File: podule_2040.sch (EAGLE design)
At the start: 58 parts, among them IC1 LT1963EST-3.3, IC2 RP2040-QFN56, IC3 SN74ALVC164245, IC4 SN74ALVC164245, U1 W25Q32FV, Y1 12MHz

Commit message: Schematic & board V1: as used for prototype fab
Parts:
- added C1: 0.1uF, rcl:C-EUC0603K
- added R12: 100K, rcl:R-EU_R0805
- added RESET: Tact sw, SparkFun-Switches:MOMENTARY-SWITCH-SPST-SMD-5.2MM-TALL
- GPIO: device SparkFun-Connectors:CONN_05 -> matt:PINHD-1X5
- J2: device SparkFun-Connectors:USB_MICRO-B_FEMALE-SMT -> SparkFun-Connectors:USB_MICRO-B_SMT
- LED1: device led:LEDCHIPLED_0805 -> led:LEDCHIPLED_1206
- SWD: device SparkFun-Connectors:CONN_04PTH -> matt:PINHD-1X4
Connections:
- removed net N$14: IC2.RUN, SWD.4
- new net RUN: C1.1, IC2.RUN, R12.1, RESET.2, SWD.4
- net +3V3: now also R12.2
- net GND: now also C1.2, RESET.1
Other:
- note added: "(c) 2021 Matt Evans"
- note added: "31 Aug 2021"
- note added: "Arc Pipe Podule"
- note added: "Licence: Creative Commons CC BY-SA 3.0 See https://creativecommons.org/licenses/by-sa/3.0/"
- note added: "v1"
- note removed: "v0.1"
- moved on the sheet: J2

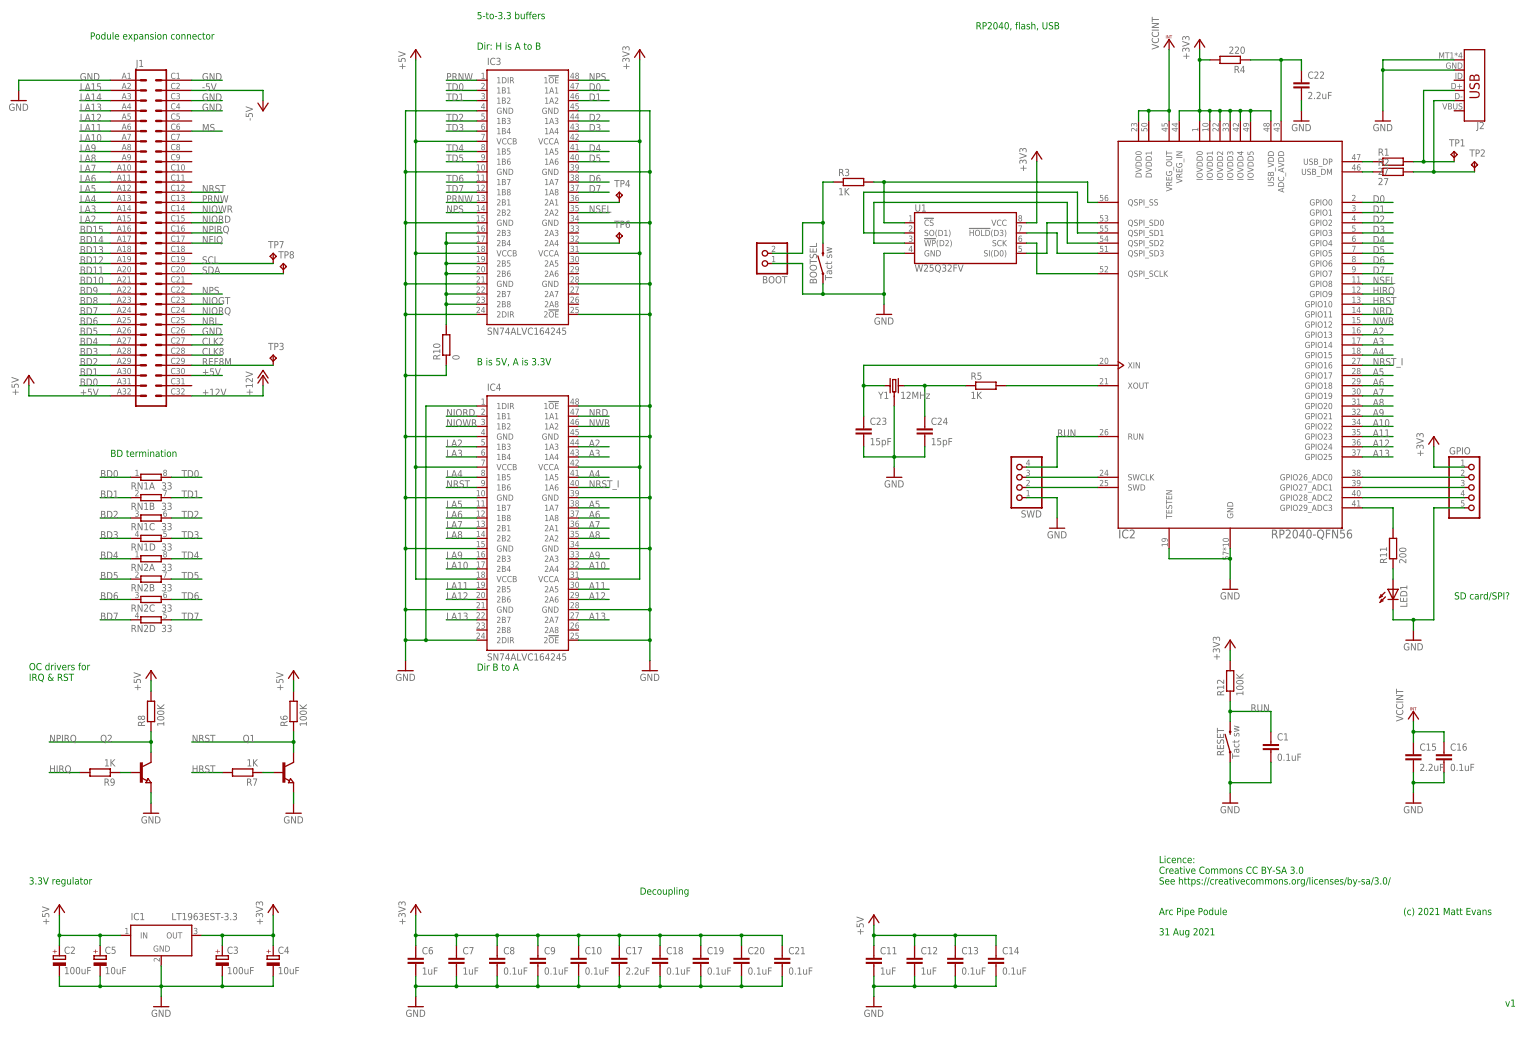
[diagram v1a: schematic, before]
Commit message: First commit of v2 design, for checking
Changes include:
- Shrink buffers to TSSOP
- Term. resistor packs on internal signals
- Removed N_RST input, freeing 4 GPIOs
- GPIOs to header, prototyping area, and added uSD footprint/resistors
- Moved QSPI closer, more decoupling, re-routed
- Brought reset/boot to a header for remote reboot
- Better labelling/silkscreen tidy, space for serial number
- More common LDO footprint
- Different crystal footprint
- Address lines contiguous
- USB VBUS can power the board, via diodes
- Flash /CS pullup footprint
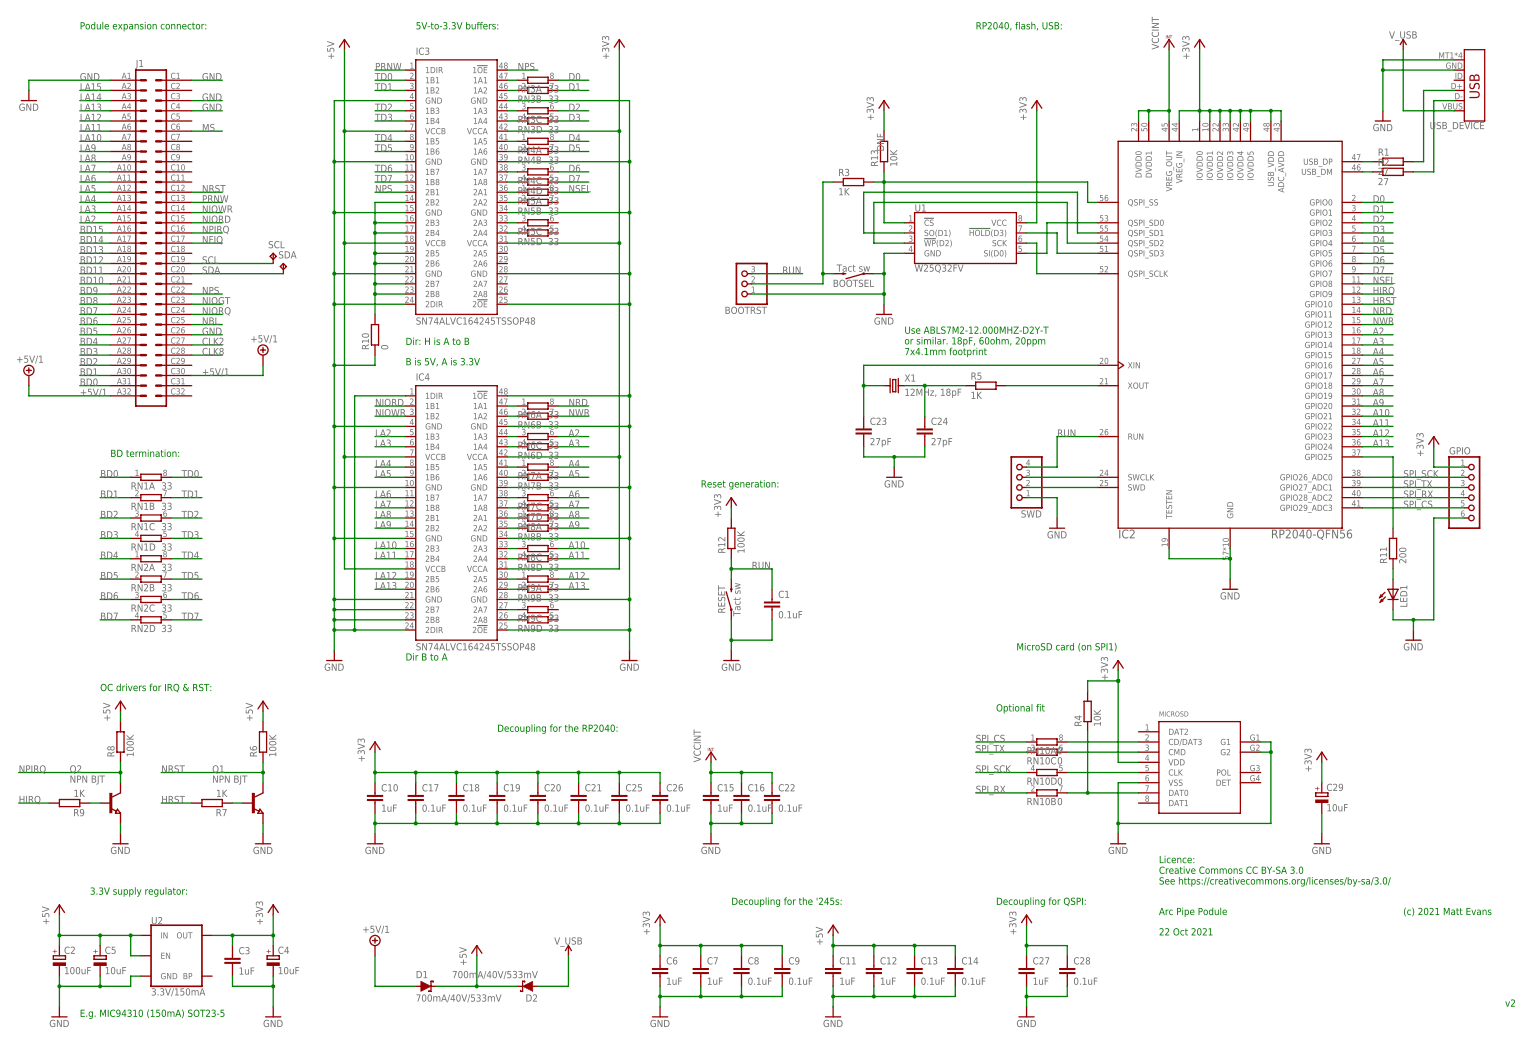
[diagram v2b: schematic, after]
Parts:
- removed BOOT: (no value), matt:PINHD-1X2
- removed IC1: LT1963EST-3.3, linear-technology:LT1963EST-3.3
- removed TP1, TP2, TP3, TP4, TP6: TPTP15R, testpad:TPTP15R
- removed Y1: 12MHz, SparkFun-Clocks:CRYSTAL-GROUNDEDSMD-5X3.2
- added BOOTRST: (no value), matt:PINHD-1X3
- added C25, C26, C28: 0.1uF, rcl:C-EUC0603K
- added C27: 1uF, rcl:C-EUC0603K
- added C29: 10uF, rcl:CPOL-EUA/3216-18W
- added D1, D2: 700mA/40V/533mV, SparkFun-DiscreteSemi:DIODE-SCHOTTKY-ZLLS500
- added MICROSD: MOLEX-USD-47309, matt:MOLEX-USD-47309
- added R13: 10K, rcl:R-EU_R0805
- added RN10: 0, resistor-dil:4R-N0603-ARC
- added RN3, RN4, RN5, RN6, RN7, RN8, RN9: 33, resistor-dil:4R-N0603-ARC
- added U2: 3.3V/150mA, SparkFun-IC-Power:V_REG_MIC52053.3V
- added X1: 12MHz, 18pF, IQD-Frequency-Products:CRYSTALS-NOGND-12SMX-A
- BOOTSEL, RESET: device SparkFun-Switches:MOMENTARY-SWITCH-SPST-SMD-5.2MM-TALL -> SparkFun-Switches:MOMENTARY-SWITCH-SPST-SMD-5.2-REDUNDANT
- C10: value 0.1uF -> 1uF
- C15: value 2.2uF -> 1uF
- C17, C22: value 2.2uF -> 0.1uF
- C23, C24: value 15pF -> 27pF
- C3: value 100uF -> 1uF; device rcl:CPOL-EUCT6032 -> rcl:C-EUC0603K
- GPIO: device matt:PINHD-1X5 -> matt:PINHD-1X6
- IC3, IC4: value SN74ALVC164245 -> SN74ALVC164245TSSOP48; device matt:SN74ALVC164245 -> matt:SN74ALVC164245TSSOP48
- Q1, Q2: value (none) -> NPN BJT
- R4: value 220 -> 10K
- renumbered J2 to USB_DEVICE, TP7 to SCL, TP8 to SDA
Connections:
- removed net +12V: J1.C32
- removed net -5V: J1.C2
- removed net N$25: GPIO.4, IC2.GPIO28_ADC2
- removed net NRST_I: IC2.GPIO16, IC4.1A6
- removed net REF8M: J1.C29, TP3.TP
- new net +5V/1: D1.A, J1.A32, J1.C30
- new net N$14: MICROSD.CD/DAT3, RN10A.2
- new net N$27: IC3.1A2, RN3B.1
- new net N$30: IC3.1A3, RN3C.1
- new net N$31: IC3.1A4, RN3D.1
- new net N$32: IC3.1A6, RN4B.1
- new net N$33: IC3.1A5, RN4A.1
- new net N$34: IC3.1A7, RN4C.1
- new net N$35: IC3.1A8, RN4D.1
- new net N$36: IC3.2A1, RN5A.1
- new net N$37: IC3.2A2, RN5B.1
- new net N$38: IC3.2A3, RN5C.1
- new net N$39: IC4.1A1, RN6A.1
- new net N$40: IC4.1A2, RN6B.1
- new net N$41: IC4.1A3, RN6C.1
- new net N$42: IC4.1A4, RN6D.1
- new net N$43: IC4.1A5, RN7A.1
- new net N$44: IC4.1A6, RN7B.1
- new net N$45: IC4.1A7, RN7C.1
- new net N$46: IC4.1A8, RN7D.1
- new net N$47: IC4.2A1, RN8A.1
- new net N$48: IC4.2A2, RN8B.1
- new net N$49: IC4.2A3, RN8C.1
- new net N$50: IC4.2A4, RN8D.1
- new net N$51: IC4.2A5, RN9A.1
- new net N$52: IC4.2A6, RN9B.1
- new net N$53: IC4.2A7, RN9C.1
- new net N$54: IC4.2A8, RN9D.1
- new net SPI_CS: GPIO.5, IC2.GPIO29_ADC3, RN10A.1
- new net SPI_RX: GPIO.4, IC2.GPIO28_ADC2, RN10B.1
- new net SPI_SCK: GPIO.2, IC2.GPIO26_ADC0, RN10D.1
- new net SPI_TX: GPIO.3, IC2.GPIO27_ADC1, RN10C.1
- new net V_USB: D2.A, USB_DEVICE.VBUS
- net +3V3: now also C25.1, C26.1, C27.1, C28.1, C29.+, C3.1, IC2.ADC_AVDD, MICROSD.VDD, R13.2, U2.OUT; no longer C3.+, IC1G$1.OUT
- net +5V: now also D1.C, D2.C, U2.EN, U2.IN; no longer IC1G$1.IN, J1.A32, J1.C30
- net A10: now also IC2.GPIO21, RN8C.2; no longer IC2.GPIO22, IC4.2A4
- net A11: now also IC2.GPIO22, RN8D.2; no longer IC2.GPIO23, IC4.2A5
- net A12: now also IC2.GPIO23, RN9A.2; no longer IC2.GPIO24, IC4.2A6
- net A13: now also IC2.GPIO24, RN9B.2; no longer IC2.GPIO25, IC4.2A7
- net A2: now also RN6C.2; no longer IC4.1A3
- net A3: now also RN6D.2; no longer IC4.1A4
- net A4: now also RN7A.2; no longer IC4.1A5
- net A5: now also IC2.GPIO16, RN7B.2; no longer IC2.GPIO17, IC4.1A7
- net A6: now also IC2.GPIO17, RN7C.2; no longer IC2.GPIO18, IC4.1A8
- net A7: now also IC2.GPIO18, RN7D.2; no longer IC2.GPIO19, IC4.2A1
- net A8: now also IC2.GPIO19, RN8A.2; no longer IC2.GPIO20, IC4.2A2
- net A9: now also IC2.GPIO20, RN8B.2; no longer IC2.GPIO21, IC4.2A3
- net D0: now also RN3A.2; no longer IC3.1A1
- net D1: now also RN3B.2; no longer IC3.1A2
- net D2: now also RN3C.2; no longer IC3.1A3
- net D3: now also RN3D.2; no longer IC3.1A4
- net D4: now also RN4A.2; no longer IC3.1A5
- net D5: now also RN4B.2; no longer IC3.1A6
- net D6: now also RN4C.2; no longer IC3.1A7
- net D7: now also RN4D.2; no longer IC3.1A8
- net GND: now also BOOTRST.1, C25.2, C26.2, C27.2, C28.2, C29.-, C3.2, GPIO.6, IC4.2B7, IC4.2B8, MICROSD.G1, MICROSD.G2, MICROSD.VSS, U2.GND; no longer BOOT.1, C3.-, GPIO.5, IC1G$1.GND, Y1.GND
- net LA10: now also IC4.2B3; no longer IC4.2B4
- net LA11: now also IC4.2B4; no longer IC4.2B5
- net LA12: now also IC4.2B5; no longer IC4.2B6
- net LA13: now also IC4.2B6; no longer IC4.2B7
- net LA5: now also IC4.1B6; no longer IC4.1B7
- net LA6: now also IC4.1B7; no longer IC4.1B8
- net LA7: now also IC4.1B8; no longer IC4.2B1
- net LA8: now also IC4.2B1; no longer IC4.2B2
- net LA9: now also IC4.2B2; no longer IC4.2B3
- net N$10: now also MICROSD.CLK, RN10D.2; no longer C22.1, IC2.ADC_AVDD, R4.1
- net N$11: now also R13.1
- net N$12: now also BOOTRST.2; no longer BOOT.2
- net N$17: now also X1.2; no longer Y1.2
- net N$19: now also X1.1; no longer Y1.1
- net N$21: now also IC3.1A1, RN3A.1; no longer IC3.2A1, TP4.TP
- net N$22: now also IC3.2B2
- net N$23: now also MICROSD.CMD, RN10C.2; no longer GPIO.2, IC2.GPIO26_ADC0
- net N$24: now also MICROSD.DAT0, R4.1, RN10B.2; no longer GPIO.3, IC2.GPIO27_ADC1
- net N$28: now also IC2.GPIO25; no longer IC2.GPIO29_ADC3
- net N$29: now also RN5D.1; no longer TP6.TP
- net N$3: no longer TP1.TP
- net N$4: no longer TP2.TP
- net NPS: now also IC3.2B1; no longer IC3.2B2
- net NRD: now also RN6A.2; no longer IC4.1A1
- net NRST: no longer IC4.1B6
- net NSEL: now also RN5A.2; no longer IC3.2A2
- net NWR: now also RN6B.2; no longer IC4.1A2
- net PRNW: no longer IC3.2B1
- net RUN: now also BOOTRST.3
- net VCCINT: now also C22.1
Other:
- note added: "22 Oct 2021"
- note added: "3.3V supply regulator:"
- note added: "5V-to-3.3V buffers:"
- note added: "BD termination:"
- note added: "Decoupling for QSPI:"
- note added: "Decoupling for the '245s:"
- note added: "Decoupling for the RP2040:"
- note added: "E.g. MIC94310 (150mA) SOT23-5"
- note added: "MicroSD card (on SPI1)"
- note added: "OC drivers for IRQ & RST:"
- note added: "Optional fit"
- note added: "Podule expansion connector:"
- note added: "RP2040, flash, USB:"
- note added: "Reset generation:"
- note added: "Use ABLS7M2-12.000MHZ-D2Y-T or similar. 18pF, 60ohm, 20ppm 7x4.1mm footprint"
- note added: "v2"
- note removed: "3.3V regulator"
- note removed: "31 Aug 2021"
- note removed: "5-to-3.3 buffers"
- note removed: "BD termination"
- note removed: "Decoupling"
- note removed: "OC drivers for IRQ & RST"
- note removed: "Podule expansion connector"
- note removed: "RP2040, flash, USB"
- note removed: "SD card/SPI?"
- note removed: "v1"
- moved on the sheet: BOOTSEL, C1, C10, C11, C12, C13, C14, C15, C16, C17, C18, C19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

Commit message: Tidy-ups for v2
Not released yet: board looks good, work needed on README etc.
Not fabricated yet.
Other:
- moved on the sheet: USB_DEVICE
